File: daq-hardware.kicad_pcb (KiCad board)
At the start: 2 copper layers, 100 x 60 mm, 7 parts, among them J1 USB_B, J2 Micro_SD_Card_Det_Hirose_DM3AT, Q1 MMDT2222A, U1 CP2102N-A01-GQFN24, U2 ESP32-WROOM-32D

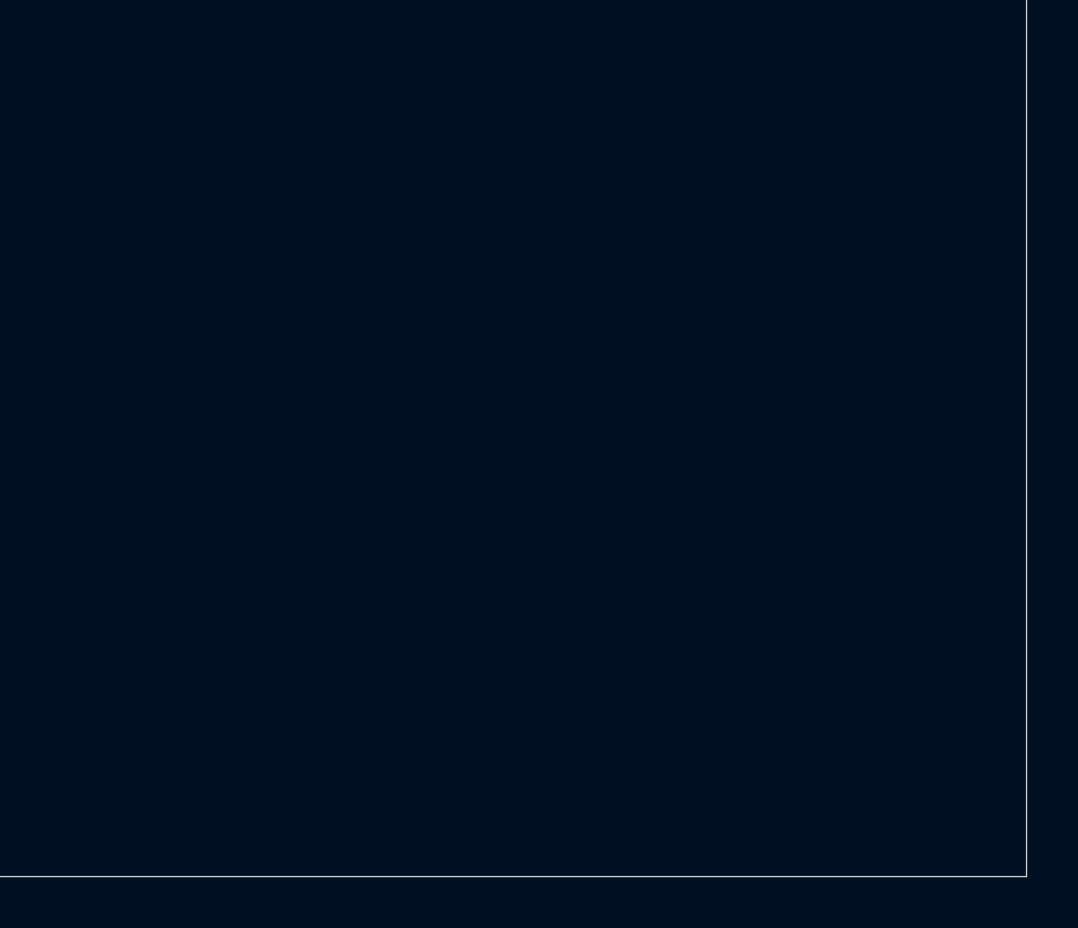
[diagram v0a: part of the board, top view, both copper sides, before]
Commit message: Thermocouples
Added components to the PCB. Please check the GND and VCC lines arrangement for any changes.
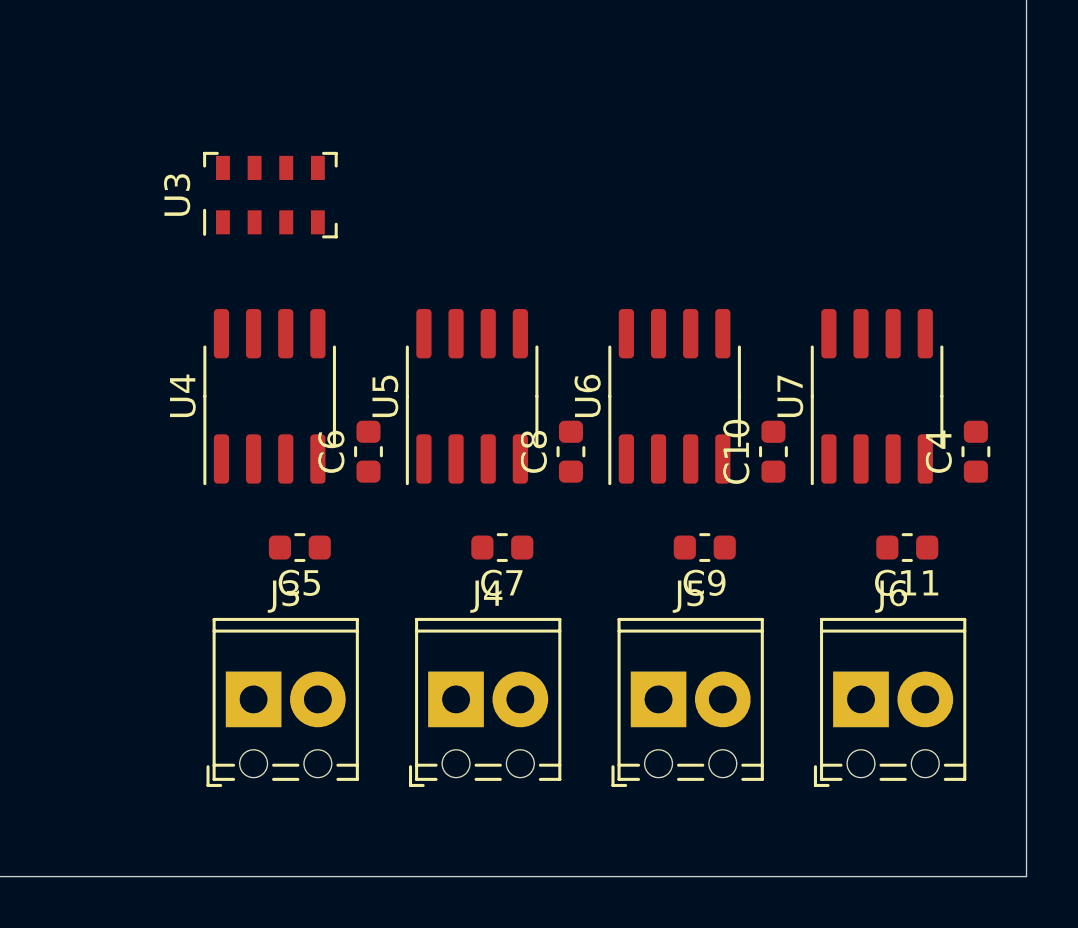
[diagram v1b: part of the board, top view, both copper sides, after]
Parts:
- added C10: 100nF, Capacitor_SMD:C_0603_1608Metric, F.Cu at (190.0, 123.2)
- added C11: 10nF, Capacitor_SMD:C_0603_1608Metric, F.Cu at (195.3, 127.0)
- added C4: 100nF, Capacitor_SMD:C_0603_1608Metric, F.Cu at (198.0, 123.2)
- added C5: 10nF, Capacitor_SMD:C_0603_1608Metric, F.Cu at (171.3, 127.0)
- added C6: 100nF, Capacitor_SMD:C_0603_1608Metric, F.Cu at (174.0, 123.2)
- added C7: 10nF, Capacitor_SMD:C_0603_1608Metric, F.Cu at (179.3, 127.0)
- added C8: 100nF, Capacitor_SMD:C_0603_1608Metric, F.Cu at (182.0, 123.2)
- added C9: 10nF, Capacitor_SMD:C_0603_1608Metric, F.Cu at (187.3, 127.0)
- added J3: Screw_Terminal_Thermo_1, TerminalBlock_Phoenix:TerminalBlock_Phoenix_MPT-0,5-2-2.54_1x02_P2.54mm_Horizontal, F.Cu at (169.5, 133.0)
- added J4: Screw_Terminal_Thermo_2, TerminalBlock_Phoenix:TerminalBlock_Phoenix_MPT-0,5-2-2.54_1x02_P2.54mm_Horizontal, F.Cu at (177.5, 133.0)
- added J5: Screw_Terminal_Thermo_3, TerminalBlock_Phoenix:TerminalBlock_Phoenix_MPT-0,5-2-2.54_1x02_P2.54mm_Horizontal, F.Cu at (185.5, 133.0)
- added J6: Screw_Terminal_Thermo_4, TerminalBlock_Phoenix:TerminalBlock_Phoenix_MPT-0,5-2-2.54_1x02_P2.54mm_Horizontal, F.Cu at (193.5, 133.0)
- added U3: MS5607-02BA, Package_LGA:LGA-8_3x5mm_P1.25mm, F.Cu at (170.1, 113.1)
- added U4: MAX31855RASA, Package_SO:SOIC-8_3.9x4.9mm_P1.27mm, F.Cu at (170.1, 121.0)
- added U5: MAX31855RASA, Package_SO:SOIC-8_3.9x4.9mm_P1.27mm, F.Cu at (178.1, 121.0)
- added U6: MAX31855RASA, Package_SO:SOIC-8_3.9x4.9mm_P1.27mm, F.Cu at (186.1, 121.0)
- added U7: MAX31855RASA, Package_SO:SOIC-8_3.9x4.9mm_P1.27mm, F.Cu at (194.1, 121.0)
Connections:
- J2 pad 1: (no net) -> Net-(J2-Pad1)
- J2 pad 10: (no net) -> Net-(J2-Pad10)
- J2 pad 2: (no net) -> /SD_CS
- J2 pad 3: (no net) -> /MOSI
- J2 pad 5: (no net) -> /SCLK
- J2 pad 7: (no net) -> /MISO
- J2 pad 8: (no net) -> Net-(J2-Pad8)
- J2 pad 9: (no net) -> Net-(J2-Pad9)
- U1 pad 1: (no net) -> Net-(U1-Pad1)
- U1 pad 10: (no net) -> Net-(U1-Pad10)
- U1 pad 11: (no net) -> Net-(U1-Pad11)
- U1 pad 12: (no net) -> Net-(U1-Pad12)
- U1 pad 13: (no net) -> Net-(U1-Pad13)
- U1 pad 14: (no net) -> Net-(U1-Pad14)
- U1 pad 15: (no net) -> Net-(U1-Pad15)
- U1 pad 16: (no net) -> Net-(U1-Pad16)
- U1 pad 17: (no net) -> Net-(U1-Pad17)
- U1 pad 18: (no net) -> Net-(U1-Pad18)
- U1 pad 19: (no net) -> Net-(U1-Pad19)
- U1 pad 22: (no net) -> Net-(U1-Pad22)
- U1 pad 23: (no net) -> Net-(U1-Pad23)
- U1 pad 24: (no net) -> Net-(U1-Pad24)
- U1 pad 8: (no net) -> Net-(R1-Pad2)
- U1 pad 9: (no net) -> Net-(U1-Pad9)
- U2 pad 10: (no net) -> Net-(U2-Pad10)
- U2 pad 11: (no net) -> Net-(U2-Pad11)
- U2 pad 12: (no net) -> Net-(U2-Pad12)
- U2 pad 13: (no net) -> Net-(U2-Pad13)
- U2 pad 14: (no net) -> Net-(U2-Pad14)
- U2 pad 16: (no net) -> Net-(U2-Pad16)
- U2 pad 17: (no net) -> Net-(U2-Pad17)
- U2 pad 18: (no net) -> Net-(U2-Pad18)
- U2 pad 19: (no net) -> Net-(U2-Pad19)
- U2 pad 20: (no net) -> Net-(U2-Pad20)
- U2 pad 21: (no net) -> Net-(U2-Pad21)
- U2 pad 22: (no net) -> Net-(U2-Pad22)
- U2 pad 23: (no net) -> Net-(U2-Pad23)
- U2 pad 24: (no net) -> Net-(U2-Pad24)
- U2 pad 26: (no net) -> Net-(U2-Pad26)
- U2 pad 27: (no net) -> Net-(U2-Pad27)
- U2 pad 28: (no net) -> Net-(U2-Pad28)
- U2 pad 29: (no net) -> /SD_CS
- U2 pad 30: (no net) -> /SCLK
- U2 pad 31: (no net) -> /MISO
- U2 pad 32: (no net) -> Net-(U2-Pad32)
- U2 pad 33: (no net) -> Net-(U2-Pad33)
- U2 pad 36: (no net) -> Net-(U2-Pad36)
- U2 pad 37: (no net) -> /MOSI
- U2 pad 4: (no net) -> Net-(U2-Pad4)
- U2 pad 5: (no net) -> Net-(U2-Pad5)
- U2 pad 6: (no net) -> /BARO_CS
- U2 pad 7: (no net) -> Net-(U2-Pad7)
- U2 pad 8: (no net) -> Net-(U2-Pad8)
- U2 pad 9: (no net) -> Net-(U2-Pad9)

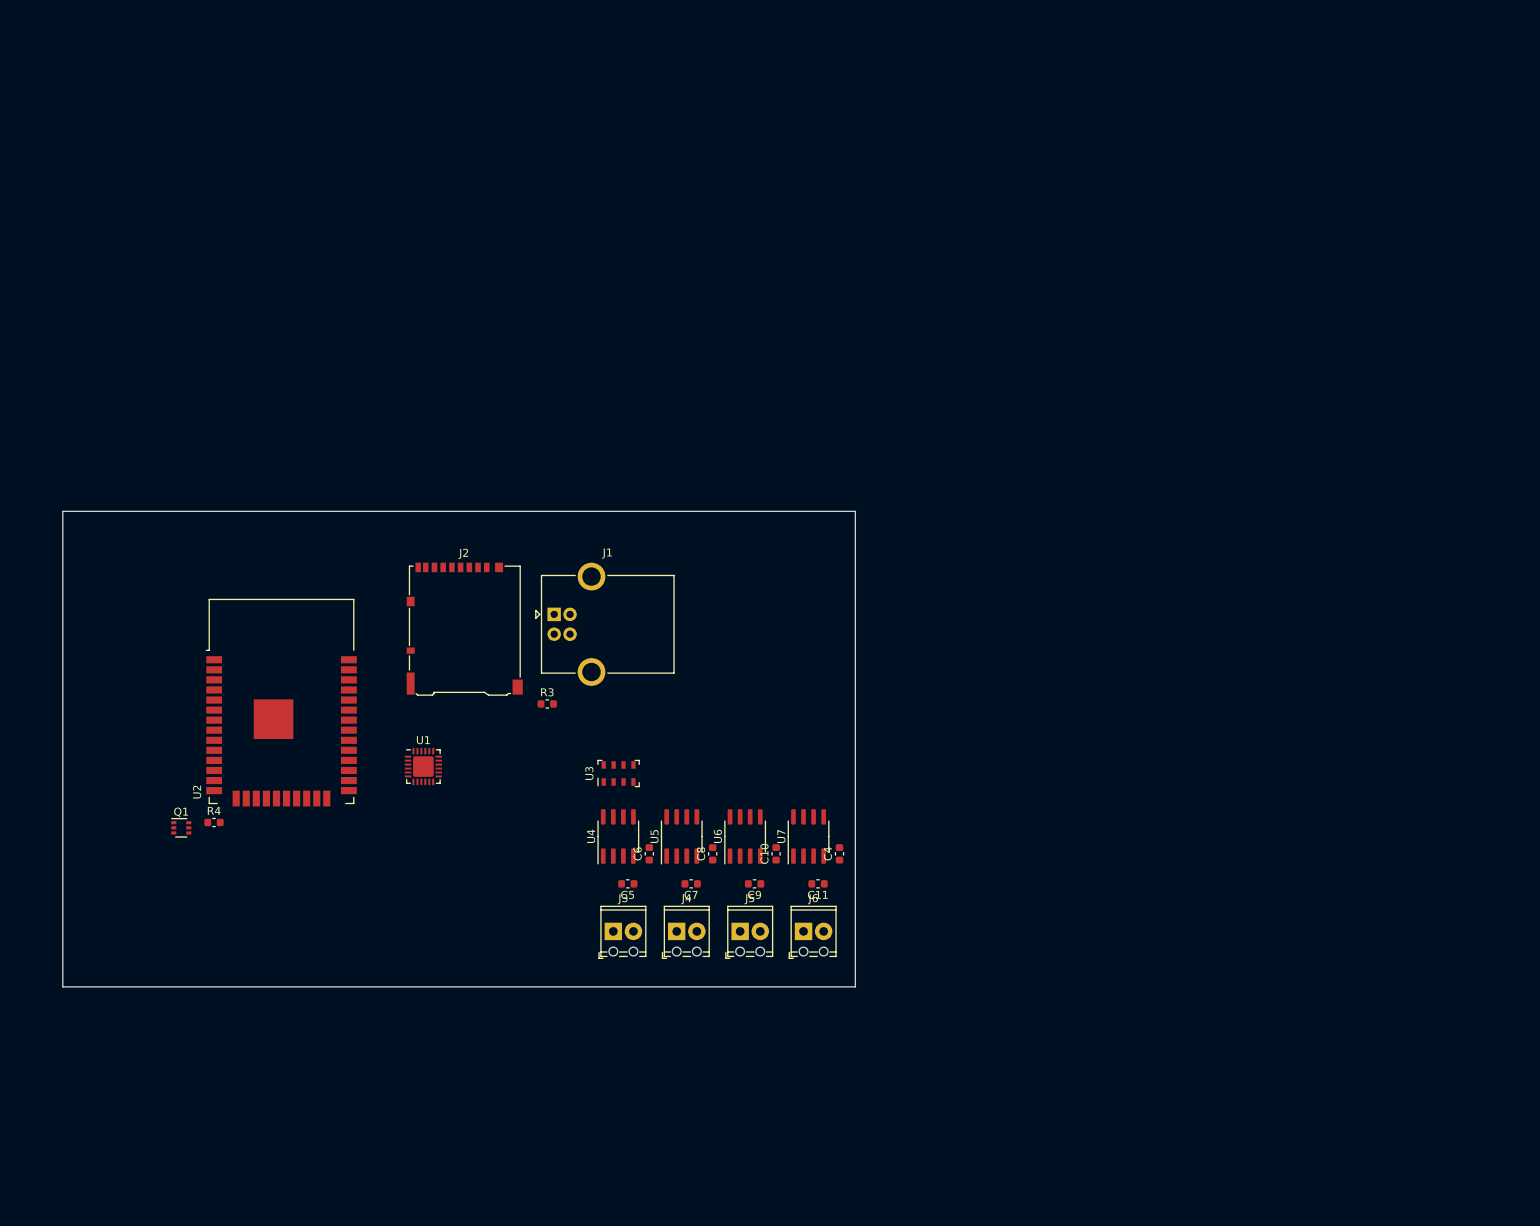
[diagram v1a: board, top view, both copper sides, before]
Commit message: Added and locked mounting holes
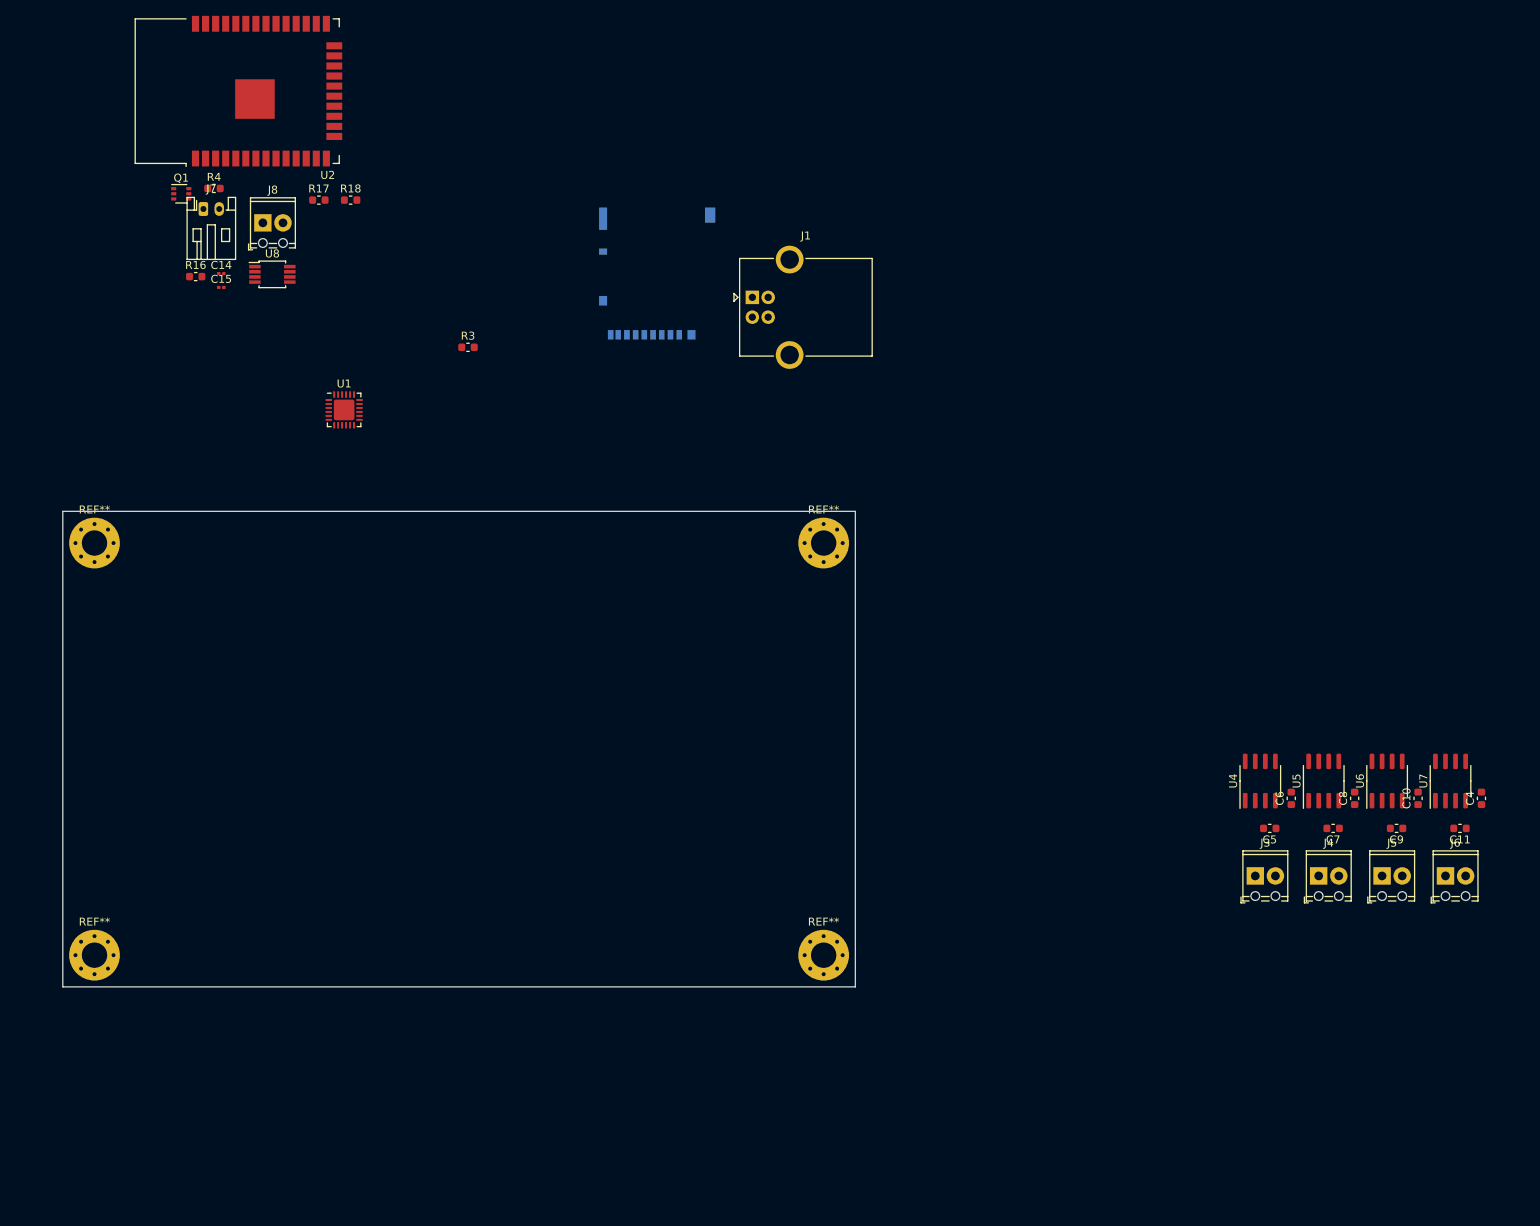
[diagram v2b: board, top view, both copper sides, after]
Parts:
- removed U3: MS5607-02BA, Package_LGA:LGA-8_3x5mm_P1.25mm
- added C14: 10u, Capacitor_SMD:C_0201_0603Metric, F.Cu at (120.0, 50.0)
- added C15: 22u, Capacitor_SMD:C_0201_0603Metric, F.Cu at (120.0, 51.8)
- added J7: Conn_01x02, Connector_JST:JST_PH_S2B-PH-K_1x02_P2.00mm_Horizontal, F.Cu at (117.7, 41.9)
- added J8: Screw_Terminal_01x02, TerminalBlock_Phoenix:TerminalBlock_Phoenix_MPT-0,5-2-2.54_1x02_P2.54mm_Horizontal, F.Cu at (125.2, 43.6)
- added R16: 100k, Resistor_SMD:R_0603_1608Metric, F.Cu at (116.8, 50.4)
- added R17: 312k5, Resistor_SMD:R_0603_1608Metric, F.Cu at (132.3, 40.7)
- added R18: 100k, Resistor_SMD:R_0603_1608Metric, F.Cu at (136.3, 40.7)
- added REF**: MountingHole_3.2mm_M3_Pad_Via, MountingHole:MountingHole_3.2mm_M3_Pad_Via, F.Cu at (196.0, 84.0)
- added REF**: MountingHole_3.2mm_M3_Pad_Via, MountingHole:MountingHole_3.2mm_M3_Pad_Via, F.Cu at (196.0, 136.0)
- added REF**: MountingHole_3.2mm_M3_Pad_Via, MountingHole:MountingHole_3.2mm_M3_Pad_Via, F.Cu at (104.0, 136.0)
- added REF**: MountingHole_3.2mm_M3_Pad_Via, MountingHole:MountingHole_3.2mm_M3_Pad_Via, F.Cu at (104.0, 84.0)
- added U8: TPS62160DGK, Package_SO:MSOP-8_3x3mm_P0.65mm, F.Cu at (126.4, 50.1)
- J2: moved to B.Cu
- moved C11 81.3 mm to (276.3, 120.0)
- moved C7 81.3 mm to (260.3, 120.0)
- moved C9 81.3 mm to (268.3, 120.0)
- moved U5 81.3 mm to (259.1, 114.0)
- moved U6 81.3 mm to (267.1, 114.0)
- moved U7 81.3 mm to (275.1, 114.0)
- moved C10 81.3 mm to (271.0, 116.2)
- moved C4 81.3 mm to (279.0, 116.2)
- moved C5 81.3 mm to (252.3, 120.0)
- moved C6 81.3 mm to (255.0, 116.2)
- moved C8 81.3 mm to (263.0, 116.2)
- moved J3 81.3 mm to (250.5, 126.0)
- moved U4 81.3 mm to (251.1, 114.0)
- moved J4 81.3 mm to (258.5, 126.0)
- moved J5 81.3 mm to (266.5, 126.0)
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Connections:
- net /GPIO0 renamed /BOOT
- J2 pad 1: Net-(J2-Pad1) -> /SD_D2
- J2 pad 10: Net-(J2-Pad10) -> (no net)
- J2 pad 11: Net-(J2-Pad11) -> GND
- J2 pad 2: /SD_CS -> /SD_D3
- J2 pad 3: /MOSI -> /SD_CMD
- J2 pad 5: /SCLK -> /SD_CLK
- J2 pad 7: /MISO -> /SD_D0
- J2 pad 8: Net-(J2-Pad8) -> /SD_D1
- J2 pad 9: Net-(J2-Pad9) -> (no net)
- U1 pad 1: Net-(U1-Pad1) -> (no net)
- U1 pad 10: Net-(U1-Pad10) -> (no net)
- U1 pad 11: Net-(U1-Pad11) -> (no net)
- U1 pad 12: Net-(U1-Pad12) -> (no net)
- U1 pad 13: Net-(U1-Pad13) -> (no net)
- U1 pad 14: Net-(U1-Pad14) -> (no net)
- U1 pad 15: Net-(U1-Pad15) -> (no net)
- U1 pad 16: Net-(U1-Pad16) -> (no net)
- U1 pad 17: Net-(U1-Pad17) -> (no net)
- U1 pad 18: Net-(U1-Pad18) -> (no net)
- U1 pad 19: Net-(U1-Pad19) -> (no net)
- U1 pad 22: Net-(U1-Pad22) -> (no net)
- U1 pad 23: Net-(U1-Pad23) -> (no net)
- U1 pad 24: Net-(U1-Pad24) -> (no net)
- U1 pad 8: Net-(R1-Pad2) -> (no net)
- U1 pad 9: Net-(U1-Pad9) -> (no net)
- U2 pad 10: Net-(U2-Pad10) -> /~TC_CS1
- U2 pad 11: Net-(U2-Pad11) -> /~TC_CS2
- U2 pad 12: Net-(U2-Pad12) -> /~TC_CS3
- U2 pad 13: Net-(U2-Pad13) -> /SD_CLK
- U2 pad 14: Net-(U2-Pad14) -> /SD_D2
- U2 pad 16: Net-(U2-Pad16) -> /SD_D3
- U2 pad 17: Net-(U2-Pad17) -> (no net)
- U2 pad 18: Net-(U2-Pad18) -> (no net)
- U2 pad 19: Net-(U2-Pad19) -> (no net)
- U2 pad 20: Net-(U2-Pad20) -> (no net)
- U2 pad 21: Net-(U2-Pad21) -> (no net)
- U2 pad 22: Net-(U2-Pad22) -> (no net)
- U2 pad 23: Net-(U2-Pad23) -> /SD_CMD
- U2 pad 24: Net-(U2-Pad24) -> /SD_D0
- U2 pad 26: Net-(U2-Pad26) -> /SD_D1
- U2 pad 27: Net-(U2-Pad27) -> (no net)
- U2 pad 28: Net-(U2-Pad28) -> (no net)
- U2 pad 29: /SD_CS -> (no net)
- U2 pad 32: Net-(U2-Pad32) -> (no net)
- U2 pad 33: Net-(U2-Pad33) -> (no net)
- U2 pad 36: Net-(U2-Pad36) -> (no net)
- U2 pad 4: Net-(U2-Pad4) -> (no net)
- U2 pad 5: Net-(U2-Pad5) -> (no net)
- U2 pad 6: /BARO_CS -> (no net)
- U2 pad 7: Net-(U2-Pad7) -> (no net)
- U2 pad 8: Net-(U2-Pad8) -> /~TC_CS4
- U2 pad 9: Net-(U2-Pad9) -> (no net)
- U4 pad 5: /thermocouples/SCLK -> /SCLK
- U4 pad 6: /thermocouples/~CS_1 -> /~TC_CS1
- U4 pad 7: /thermocouples/MISO -> /MISO
- U5 pad 5: /thermocouples/SCLK -> /SCLK
- U5 pad 6: /thermocouples/~CS_3 -> /~TC_CS3
- U5 pad 7: /thermocouples/MISO -> /MISO
- U6 pad 5: /thermocouples/SCLK -> /SCLK
- U6 pad 6: /thermocouples/~CS_2 -> /~TC_CS2
- U6 pad 7: /thermocouples/MISO -> /MISO
- U7 pad 5: /thermocouples/SCLK -> /SCLK
- U7 pad 6: /thermocouples/~CS_4 -> /~TC_CS4
- U7 pad 7: /thermocouples/MISO -> /MISO
